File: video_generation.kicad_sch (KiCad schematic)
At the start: 47 parts, among them U2 74LS32

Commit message: Edited some notes
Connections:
- net ~{PIXEL_EN} renamed ~{CHAR_EN}
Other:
- note added: "Always enabled and never resetted"
- note added: "Character clock generator"
- note added: "Handling horizontal stretch attribute: - When stretch attribute is 0, the shift register is always enabled; - When stretch attribute is 1, the shift register is enabled one clock in two."
- note added: "Invert is attribute 0: when is set, frame is displayed in inverted colors."
- note added: "Then, character is sampled for each character in J14 shift register. Attributes are sampled for each character in register K12. Note: ~{CHAR_EN} period is doubled when horizontal stretch is requested. For this reason both attributes and character must be freezed with PIXEL_EN."
- note added: "This latch is used to generate a syncronization signal, set by the VSYNC from CRTC, resetted by a read access to CRTC from Z80."
- note added: "blink is attribute 1: - when 0, it gates blink_timer and dot_pattern is not affected. - when 1, blink_timer can gate dot_pattern, making the character appear and disappear. blink_timer is a square wave obtained from VSYNC / 32 ~ 1.28s"
- note added: "show is generated by attribute index (attributes 4-6). It is always set, unless if index=100."
- note added: "underline is generated by attribute index (attributes 4-6). It can add underline, overline, both, or a blinking underline (combined with blink_underline signal). Note that "underline" is not affected by "blink" nor "show", hereby the presence of blink_underline."
- note removed: "Always enabled"
- note removed: "D0 from attribute RAM is "invert": when 1, frame is displayed in inverted colors."
- note removed: "D5 from ROM is "show": when 0, it gates dot_pattern video signal from the shift register. D1 from ROM is "blink": - when 0, it gates blink_timer and dot_pattern is not affected. - when 1, blink_timer can gate dot_pattern, making the character appear and disappear. blink_timer is a square wave obtained from VSYNC / 32 ~ 1.28s"
- note removed: "D6 from ROM is "underline" ROM is both addressed with raster address wires (RA) and some attribute RAM outputs. When attribute RAM D4 = 1 we have this D6 from ROM = 1 on RA=13, else 0, resulting in an undeline effect. Note that "underline" is not affected by "blink" nor "show". D7 from ROM must be set to make the cursor blink too."
- note removed: "Handling "stretch attribute": - When stretch attribute is 0, the shift register is always enabled; - When stretch attribute is 1, the shift register is enabled one clock in two."
- note removed: "Never resetted"
- note removed: "Then, character is sampled for each character in xx shift register. Attributes are sampled for each character in register K12. Note: ~{PIXEL_EN} period is doubled when horizontal stretch is requested. For this reason both attributes and character must be freezed with PIXEL_EN."
- note removed: "This latch is used to generate a syncronization signal, setted by the VSYNC from CRTC, resetted by a read access to CRTC from Z80."
- moved on the sheet: C52, C53, C54, R56, R57, UK15A, UK15B, UK15C, XTAL3

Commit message: Notes in kicad's sheet text blocks
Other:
- company: (none) -> Logic Systems Int'l Inc
- title: Video Generation -> CEDA - Sanco 8003 schematics
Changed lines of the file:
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@@
   (paper "A3")
   (title_block
-    (title "Video Generation")
+    (title "CEDA - Sanco 8003 schematics")
     (date "2022-05-29")
     (rev "05")
-    (comment 1 "retrofficina.glgprograms.it")
+    (company "Logic Systems Int'l Inc")
+    (comment 1 "reversed by RetrOfficina - retrofficina.glgprograms.it")
+    (comment 4 "Video Generation")
   )
   (junction (at 100.33 128.27) (diameter 0) (color 0 0 0 0)

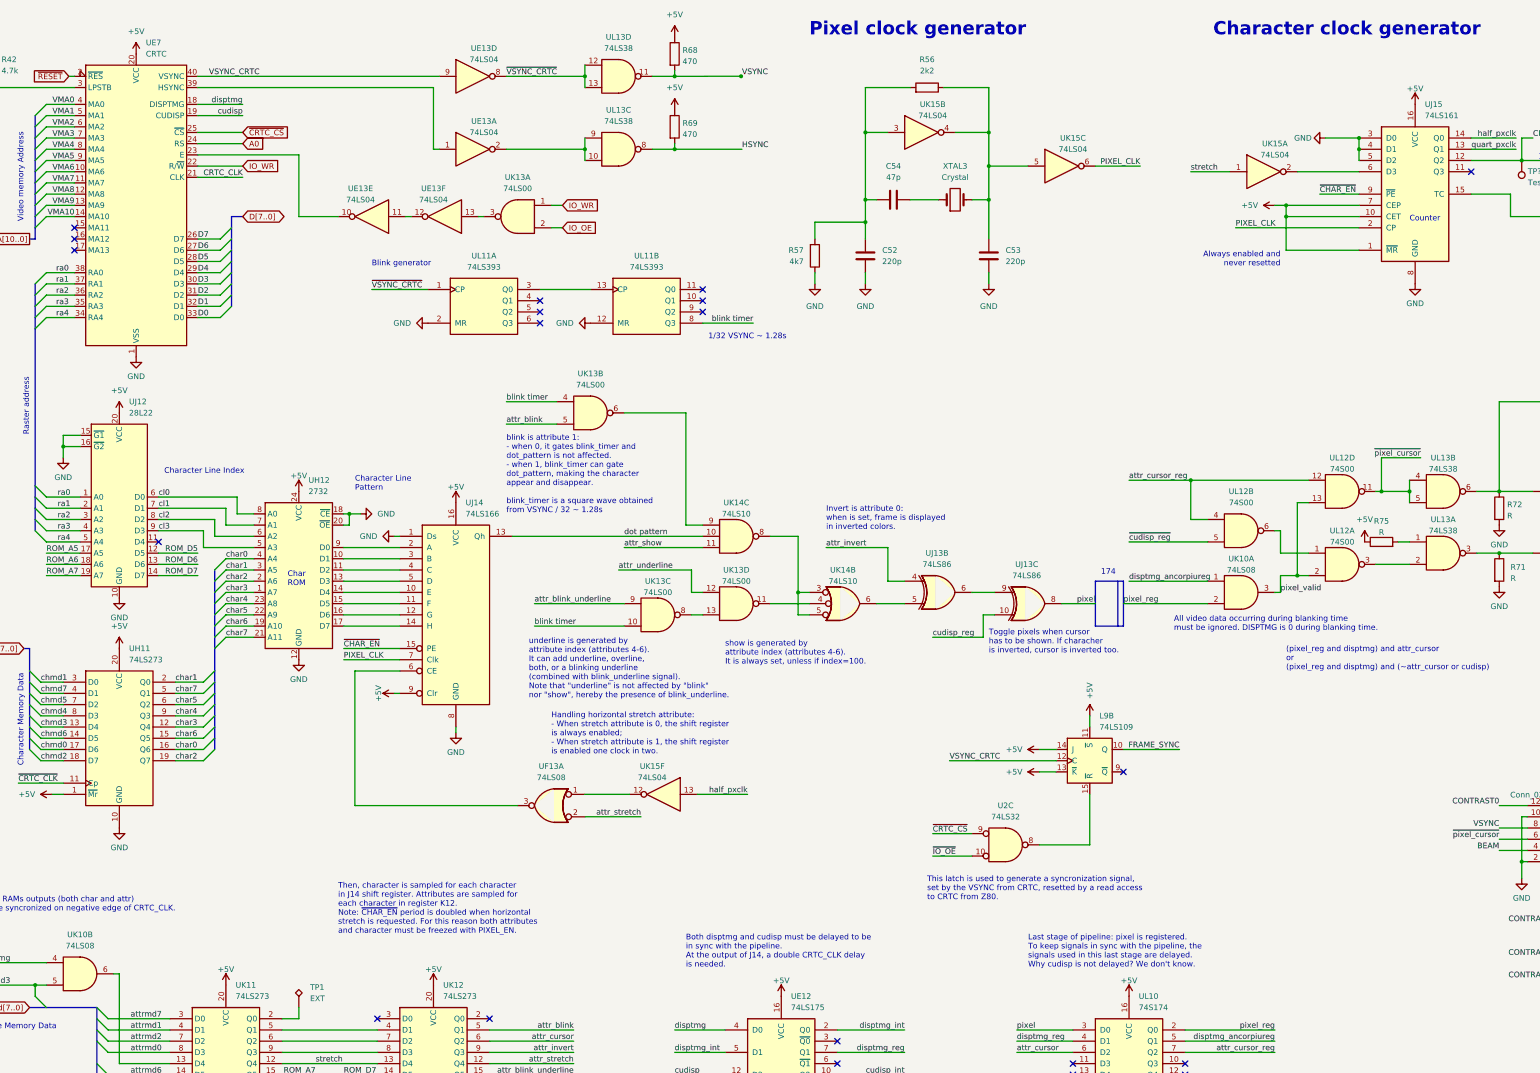
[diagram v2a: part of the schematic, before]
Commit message: Upgrade to KiCAD 9.0
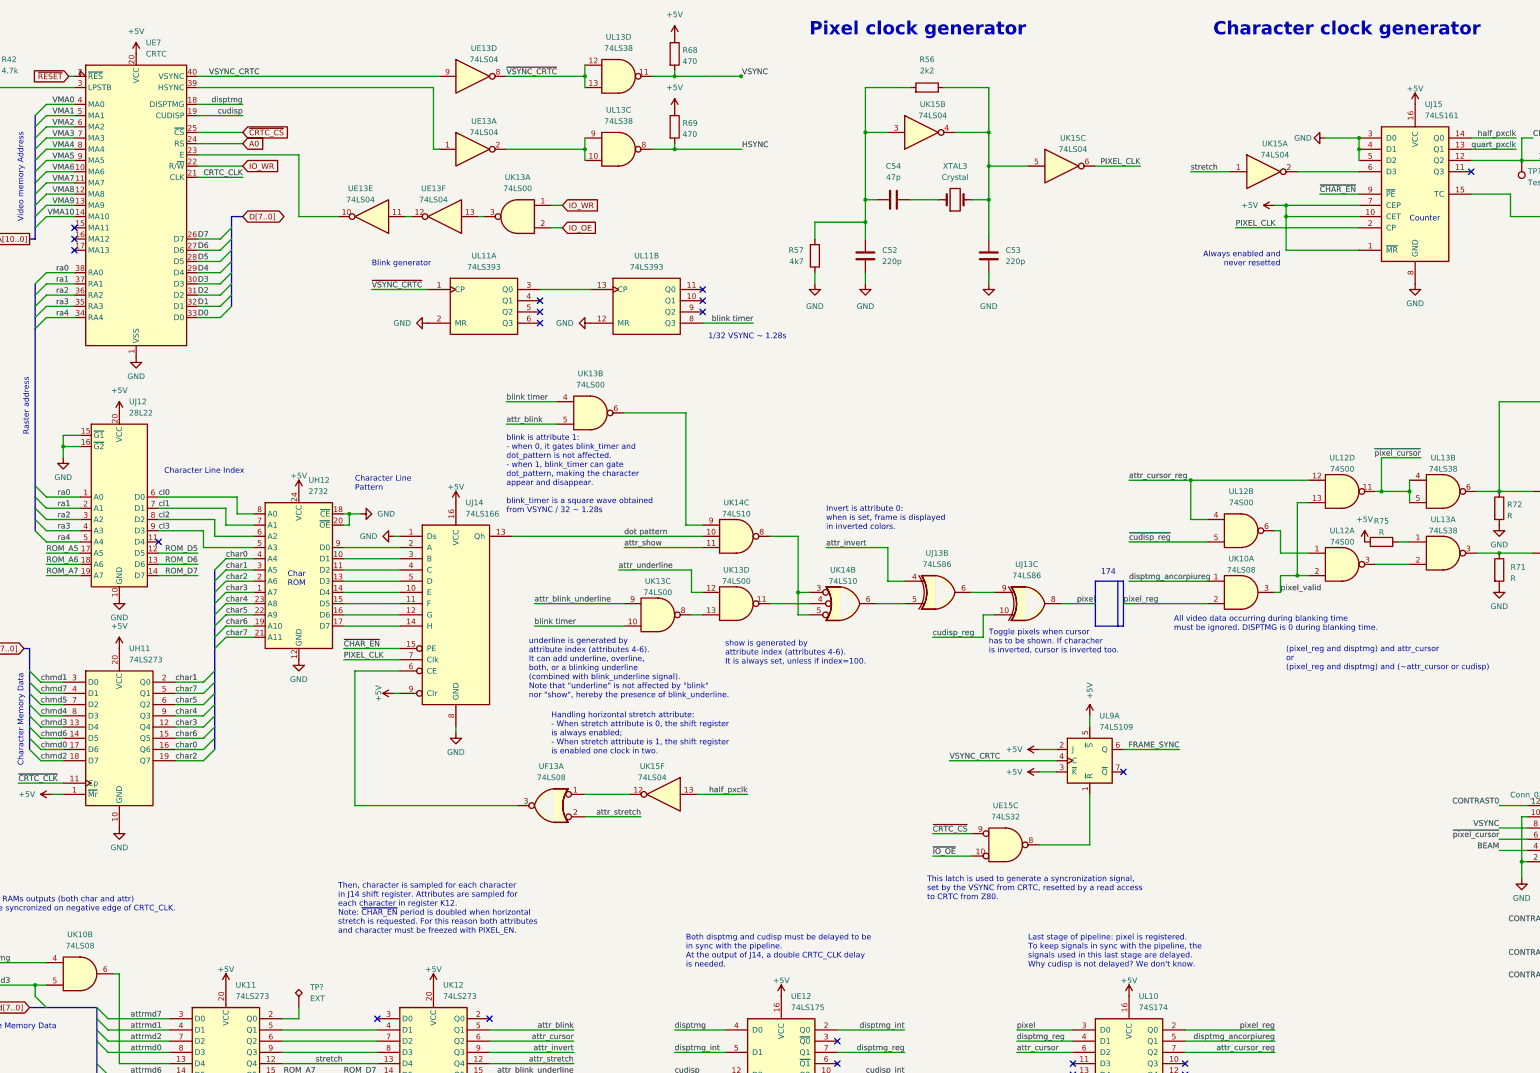
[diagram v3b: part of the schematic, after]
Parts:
- renumbered TP1 to TP?, U2 to UE15, L9 to UL9
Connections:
- net +5V: now also UL9.2 (J), UL9.3 (~{K}), UL9.5 (~{S}); no longer UL9.11 (~{S}), UL9.13 (~{K}), UL9.14 (J)
- net FRAME_SYNC: now also UL9.6 (Q); no longer UL9.10 (Q)
- net VSYNC_CRTC: now also UL9.4 (C); no longer UL9.12 (C)
- net at UE15.8: now also UL9.1 (~{R}); no longer UL9.15 (~{R})

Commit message: drc: fixed labels
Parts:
- UK13: symbol 74xx:74LS38 -> 74xx:74LS00
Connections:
- net IO_OE is gone; now on net ~{IO_OE}: UK13.2
- net IO_WR renamed ~{IO_WR}
- no-connect marks 23 -> 24
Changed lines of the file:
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@@
 	)
 	(no_connect
+		(at 379.73 204.47)
+	)
+	(no_connect
 		(at 143.51 85.09)
 	)
@@
 	(wire
 		(pts
+			(xy 389.89 22.86) (xy 377.19 22.86)
+		)
+		(stroke
+			(width 0)
+			(type default)
+		)
+	)
+	(wire
+		(pts
 			(xy 204.47 151.13) (xy 201.93 151.13)
 		)
@@
 	(wire
 		(pts
+			(xy 389.89 25.4) (xy 377.19 25.4)
+		)
+		(stroke
+			(width 0)
+			(type default)
+		)
+	)
+	(wire
+		(pts
 			(xy 72.39 138.43) (xy 78.74 138.43)
 		)
@@
 	(wire
 		(pts
+			(xy 377.19 27.94) (xy 389.89 27.94)
+		)
+		(stroke
+			(width 0)
+			(type default)
+		)
+	)
+	(wire
+		(pts
 			(xy 101.6 163.83) (xy 101.6 194.31)
 		)
@@
 		)
 	)
+	(label "half_pxclk"
+		(at 377.19 22.86 0)
+		(effects
+			(font
+				(size 1.27 1.27)
+			)
+			(justify left bottom)
+		)
+	)
 	(label "attr_blink"
 		(at 135.89 107.95 0)
@@
 		)
 	)
-	(label "~{IO_OE}"
+	(label "~{io_oe}"
 		(at 232.41 205.74 0)
 		(effects
@@
 		)
 	)
+	(label "CRTC_CLK"
+		(at 377.19 27.94 0)
+		(effects
+			(font
+				(size 1.27 1.27)
+			)
+			(justify left bottom)
+		)
+	)
 	(label "char0"
 		(at 72.39 138.43 0)
@@
 		)
 	)
-	(label "FRAME_SYNC"
+	(label "frame_sync"
 		(at 288.29 181.61 180)
 		(effects
@@
 		)
 	)
+	(label "quart_pxclk"
+		(at 377.19 25.4 0)
+		(effects
+			(font
+				(size 1.27 1.27)
+			)
+			(justify left bottom)
+		)
+	)
 	(label "half_pxclk"
 		(at 190.5 191.77 180)
@@
 		)
 	)
-	(global_label "IO_OE"
+	(global_label "~{IO_OE}"
+		(shape input)
+		(at 232.41 205.74 180)
+		(fields_autoplaced yes)
+		(effects
+			(font
+				(size 1.27 1.27)
+			)
+			(justify right)
+		)
+		(property "Intersheetrefs" "${INTERSHEET_REFS}"
+			(at 224.0424 205.74 0)
+			(effects
+				(font
+					(size 1.27 1.27)
+				)
+				(justify right)
+				(hide yes)
+			)
+		)
+	)
+	(global_label "~{IO_OE}"
 		(shape input)
 		(at 148.59 63.5 0)
@@
 		)
 	)
+	(global_label "quart_pxclk"
+		(shape output)
+		(at 389.89 25.4 0)
+		(effects
+			(font
+				(size 1.27 1.27)
+			)
+			(justify left)
+		)
+		(property "Intersheetrefs" "${INTERSHEET_REFS}"
+			(at 393.6007 25.4 0)
+			(effects
+				(font
+					(size 1.27 1.27)
+				)
+				(justify left)
+				(hide yes)
+			)
+		)
+	)
 	(global_label "attrmd[7..0]"
 		(shape input)
@@
 		)
 	)
-	(global_label "IO_WR"
+	(global_label "CRTC_CLK"
+		(shape output)
+		(at 389.89 27.94 0)
+		(fields_autoplaced yes)
+		(effects
+			(font
+				(size 1.27 1.27)
+			)
+			(justify left)
+		)
+		(property "Intersheetrefs" "${INTERSHEET_REFS}"
+			(at 402.1885 27.94 0)
+			(effects
+				(font
+					(size 1.27 1.27)
+				)
+				(justify left)
+				(hide yes)
+			)
+		)
+	)
+	(global_label "~{IO_WR}"
 		(shape input)
 		(at 148.59 58.42 0)
@@
 		)
 	)
-	(global_label "IO_WR"
+	(global_label "~{IO_WR}"
 		(shape input)
 		(at 76.2 49.53 0)
@@
 		)
 	)
+	(global_label "FRAME_SYNC"
+		(shape output)
+		(at 288.29 181.61 0)
+		(fields_autoplaced yes)
+		(effects
+			(font
+				(size 1.27 1.27)
+			)
+			(justify left)
+		)
+		(property "Intersheetrefs" "${INTERSHEET_REFS}"
+			(at 303.189 181.61 0)
+			(effects
+				(font
+					(size 1.27 1.27)
+				)
+				(justify left)
+				(hide yes)
+			)
+		)
+	)
 	(global_label "~{RESET}"
 		(shape input)
@@
 		)
 	)
+	(global_label "half_pxclk"
+		(shape output)
+		(at 389.89 22.86 0)
+		(effects
+			(font
+				(size 1.27 1.27)
+			)
+			(justify left)
+		)
+		(property "Intersheetrefs" "${INTERSHEET_REFS}"
+			(at 392.3307 22.86 0)
+			(effects
+				(font
+					(size 1.27 1.27)
+				)
+				(justify left)
+				(hide yes)
+			)
+		)
+	)
 	(symbol
 		(lib_id "74xx:74LS04")
@@
 			)
 		)
-		(property "Description" ""
+		(property "Description" "quad 2-input NAND gate"
 			(at 154.94 105.41 0)
 			(effects
@@
 					(size 1.27 1.27)
 				)
+				(hide yes)
 			)
 		)
@@
 			)
 		)
-		(property "Description" ""
+		(property "Description" "quad 2-input NAND gate"
 			(at 187.96 148.59 0)
 			(effects
@@
 					(size 1.27 1.27)
 				)
+				(hide yes)
 			)
 		)
@@
 			)
 		)
-		(property "Description" ""
+		(property "Description" "quad 2-input NAND gate"
 			(at 170.18 151.13 0)
 			(effects
@@
 					(size 1.27 1.27)
 				)
+				(hide yes)
 			)
 		)
@@
 	)
 	(symbol
-		(lib_id "74xx:74LS38")
+		(lib_id "74xx:74LS00")
 		(at 138.43 60.96 0)
 		(mirror y)
@@
 			)
 		)
-		(property "Datasheet" "http://www.ti.com/lit/gpn/sn74LS38"
-			(at 181.61 0 0)
+		(property "Datasheet" "http://www.ti.com/lit/gpn/sn74ls00"
+			(at 138.43 60.96 0)
 			(effects
 				(font
@@
 			)
 		)
-		(property "Description" ""
+		(property "Description" "quad 2-input NAND gate"
 			(at 138.43 60.96 0)
 			(effects
@@
 					(size 1.27 1.27)
 				)
+				(hide yes)
 			)
 		)

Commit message: Annotated all components
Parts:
- gave numbers to parts that had none: 3
- renumbered R71 to R39, RCK to RCK1
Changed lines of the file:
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@@
 		(dnp no)
 		(fields_autoplaced yes)
-		(property "Reference" "TP?"
+		(property "Reference" "TP5"
 			(at 367.157 50.7273 0)
 			(effects
@@
 			(project "ceda"
 				(path "/12a6dbe3-008d-4c5b-88f6-9f1c816060be/ce60e45b-d802-4380-8f39-bef3de5fa20e"
-					(reference "TP?")
+					(reference "TP5")
 					(unit 1)
 				)
@@
 		(dnp no)
 		(fields_autoplaced yes)
-		(property "Reference" "R71"
-			(at 381.508 116.0053 0)
+		(property "Reference" "R39"
+			(at 382.27 115.5699 0)
 			(effects
 				(font
@@
 		)
 		(property "Value" "R"
-			(at 381.508 118.5422 0)
+			(at 382.27 118.1099 0)
 			(effects
 				(font
@@
 			(project "ceda"
 				(path "/12a6dbe3-008d-4c5b-88f6-9f1c816060be/ce60e45b-d802-4380-8f39-bef3de5fa20e"
-					(reference "R71")
+					(reference "R39")
 					(unit 1)
 				)
@@
 		(dnp no)
 		(fields_autoplaced yes)
-		(property "Reference" "TP?"
+		(property "Reference" "TP4"
 			(at 91.44 235.458 0)
 			(effects
@@
 			(project "ceda"
 				(path "/12a6dbe3-008d-4c5b-88f6-9f1c816060be/ce60e45b-d802-4380-8f39-bef3de5fa20e"
-					(reference "TP?")
+					(reference "TP4")
 					(unit 1)
 				)
@@
 		(dnp no)
 		(fields_autoplaced yes)
-		(property "Reference" "RCK"
+		(property "Reference" "RCK1"
 			(at 382.905 223.9553 0)
 			(effects
@@
 			(project "ceda"
 				(path "/12a6dbe3-008d-4c5b-88f6-9f1c816060be/ce60e45b-d802-4380-8f39-bef3de5fa20e"
-					(reference "RCK")
+					(reference "RCK1")
 					(unit 1)
 				)
@@
 		(dnp no)
 		(fields_autoplaced yes)
-		(property "Reference" "J?"
+		(property "Reference" "J3"
 			(at 373.38 189.3402 0)
 			(effects
@@
 			(project "ceda"
 				(path "/12a6dbe3-008d-4c5b-88f6-9f1c816060be/ce60e45b-d802-4380-8f39-bef3de5fa20e"
-					(reference "J?")
+					(reference "J3")
 					(unit 1)
 				)
